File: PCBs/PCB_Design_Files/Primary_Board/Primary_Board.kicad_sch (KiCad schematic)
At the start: 6 parts, among them J1 Conn_FFC_8pin, J2 Conn_01x08_Pin

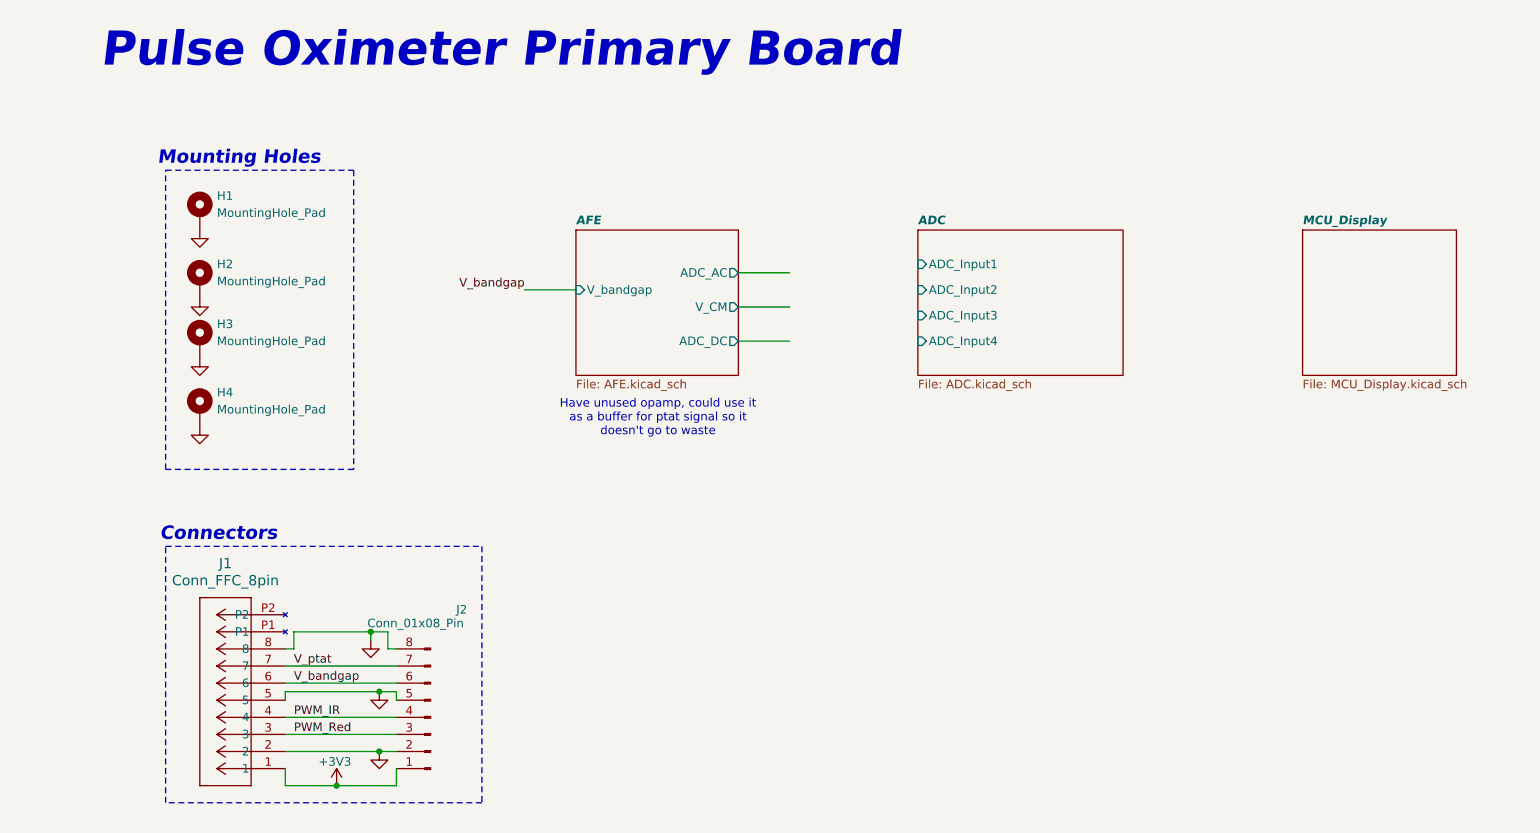
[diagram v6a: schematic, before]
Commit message: ADC schematic done
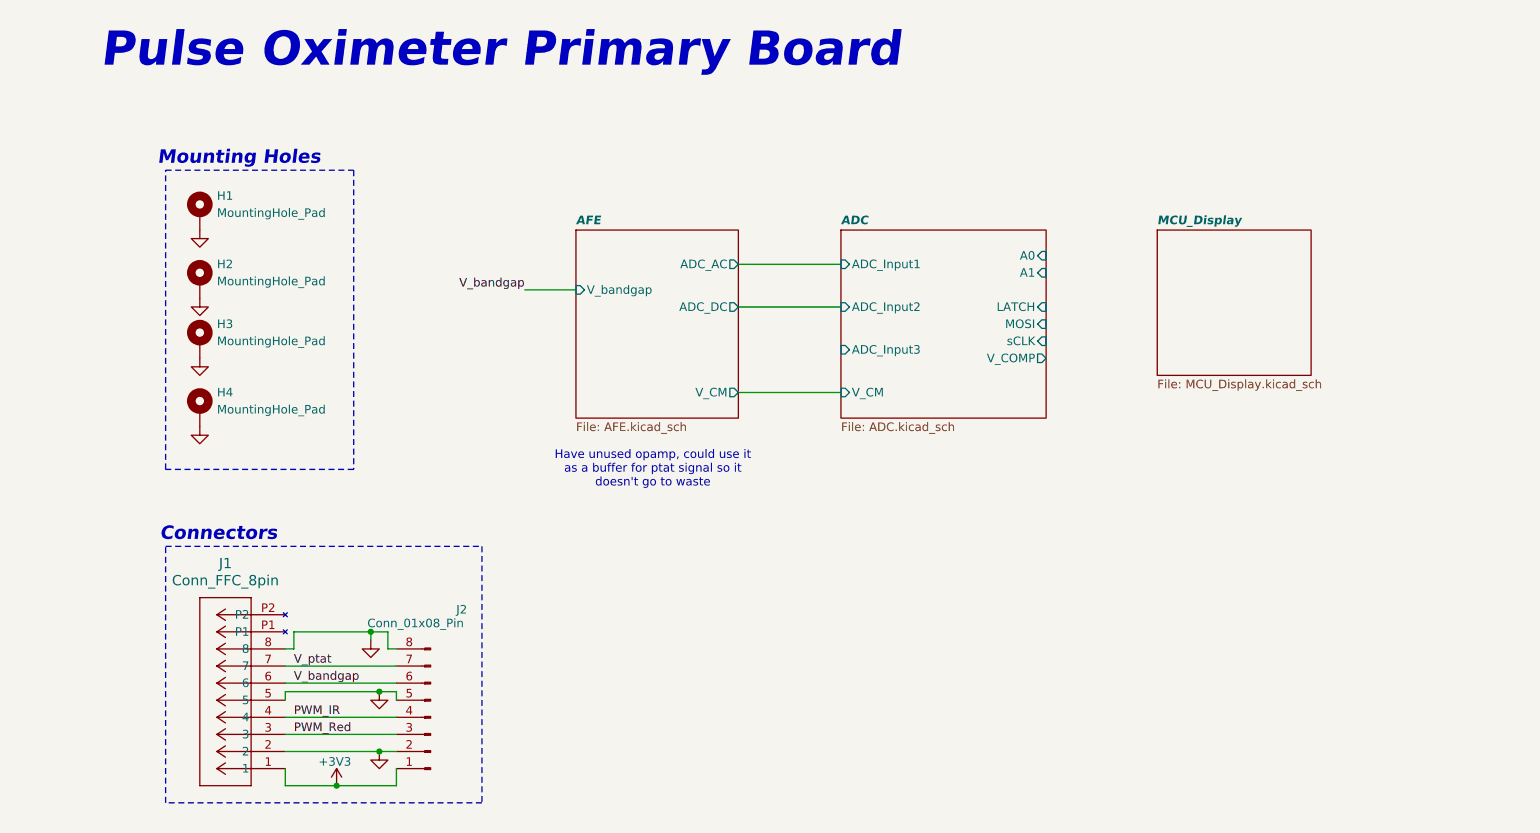
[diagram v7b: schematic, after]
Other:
- sheet ADC ports: added A0, A1, LATCH, MOSI, V_CM, V_COMP, sCLK; removed ADC_Input4
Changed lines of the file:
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@@
 	(text "Have unused opamp, could use it\nas a buffer for ptat signal so it\ndoesn't go to waste"
 		(exclude_from_sim no)
-		(at 98.552 74.93 0)
+		(at 97.79 82.55 0)
 		(effects
 			(font
@@
 	(wire
 		(pts
+			(xy 78.74 55.88) (xy 86.36 55.88)
+		)
+		(stroke
+			(width 0)
+			(type default)
+		)
+	)
+	(wire
+		(pts
 			(xy 43.18 109.22) (xy 44.45 109.22)
 		)
@@
 	(wire
 		(pts
+			(xy 110.49 58.42) (xy 125.73 58.42)
+		)
+		(stroke
+			(width 0)
+			(type default)
+		)
+	)
+	(wire
+		(pts
 			(xy 58.42 106.68) (xy 58.42 109.22)
 		)
@@
 	(wire
 		(pts
-			(xy 110.49 63.5) (xy 118.11 63.5)
-		)
-		(stroke
-			(width 0)
-			(type default)
-		)
-	)
-	(wire
-		(pts
 			(xy 43.18 114.3) (xy 59.69 114.3)
 		)
@@
 	(wire
 		(pts
-			(xy 78.74 55.88) (xy 86.36 55.88)
-		)
-		(stroke
-			(width 0)
-			(type default)
-		)
-	)
-	(wire
-		(pts
-			(xy 110.49 58.42) (xy 118.11 58.42)
+			(xy 110.49 71.12) (xy 125.73 71.12)
+		)
+		(stroke
+			(width 0)
+			(type default)
+		)
+	)
+	(wire
+		(pts
+			(xy 110.49 52.07) (xy 125.73 52.07)
 		)
 		(stroke
@@
 		(pts
 			(xy 43.18 121.92) (xy 59.69 121.92)
-		)
-		(stroke
-			(width 0)
-			(type default)
-		)
-	)
-	(wire
-		(pts
-			(xy 110.49 53.34) (xy 118.11 53.34)
 		)
 		(stroke
@@
 	(sheet
 		(at 86.36 46.99)
-		(size 24.13 21.59)
+		(size 24.13 27.94)
 		(exclude_from_sim no)
 		(in_bom yes)
@@
 		)
 		(property "Sheetfile" "AFE.kicad_sch"
-			(at 86.36 69.1646 0)
+			(at 86.36 75.5146 0)
 			(effects
 				(font
@@
 		)
 		(pin "ADC_AC" output
-			(at 110.49 53.34 0)
+			(at 110.49 52.07 0)
 			(effects
 				(font
@@
 		)
 		(pin "ADC_DC" output
-			(at 110.49 63.5 0)
+			(at 110.49 58.42 0)
 			(effects
 				(font
@@
 		)
 		(pin "V_CM" output
-			(at 110.49 58.42 0)
+			(at 110.49 71.12 0)
 			(effects
 				(font
@@
 	)
 	(sheet
-		(at 137.16 46.99)
-		(size 30.48 21.59)
+		(at 125.73 46.99)
+		(size 30.48 27.94)
 		(exclude_from_sim no)
 		(in_bom yes)
@@
 		)
 		(property "Sheetname" "ADC"
-			(at 137.16 46.2784 0)
+			(at 125.73 46.2784 0)
 			(effects
 				(font
@@
 		)
 		(property "Sheetfile" "ADC.kicad_sch"
-			(at 137.16 69.1646 0)
+			(at 125.73 75.5146 0)
 			(effects
 				(font
@@
 		)
 		(pin "ADC_Input1" input
-			(at 137.16 52.07 180)
+			(at 125.73 52.07 180)
 			(effects
 				(font
@@
 		)
 		(pin "ADC_Input2" input
-			(at 137.16 55.88 180)
+			(at 125.73 58.42 180)
 			(effects
 				(font
@@
 		)
 		(pin "ADC_Input3" input
-			(at 137.16 59.69 180)
+			(at 125.73 64.77 180)
 			(effects
 				(font
@@
 			)
 		)
-		(pin "ADC_Input4" input
-			(at 137.16 63.5 180)
+		(pin "A0" input
+			(at 156.21 50.8 0)
+			(effects
+				(font
+					(size 1.27 1.27)
+				)
+				(justify right)
+			)
+		)
+		(pin "A1" input
+			(at 156.21 53.34 0)
+			(effects
+				(font
+					(size 1.27 1.27)
+				)
+				(justify right)
+			)
+		)
+		(pin "LATCH" input
+			(at 156.21 58.42 0)
+			(effects
+				(font
+					(size 1.27 1.27)
+				)
+				(justify right)
+			)
+		)
+		(pin "MOSI" input
+			(at 156.21 60.96 0)
+			(effects
+				(font
+					(size 1.27 1.27)
+				)
+				(justify right)
+			)
+		)
+		(pin "sCLK" input
+			(at 156.21 63.5 0)
+			(effects
+				(font
+					(size 1.27 1.27)
+				)
+				(justify right)
+			)
+		)
+		(pin "V_CM" input
+			(at 125.73 71.12 180)
 			(effects
 				(font
@@
 				)
 				(justify left)
+			)
+		)
+		(pin "V_COMP" output
+			(at 156.21 66.04 0)
+			(effects
+				(font
+					(size 1.27 1.27)
+				)
+				(justify right)
 			)
 		)
@@
 	)
 	(sheet
-		(at 194.31 46.99)
+		(at 172.72 46.99)
 		(size 22.86 21.59)
 		(exclude_from_sim no)
@@
 		)
 		(property "Sheetname" "MCU_Display"
-			(at 194.31 46.2784 0)
+			(at 172.72 46.2784 0)
 			(effects
 				(font
@@
 		)
 		(property "Sheetfile" "MCU_Display.kicad_sch"
-			(at 194.31 69.1646 0)
-			(effects
-				(font
+			(at 172.72 69.1646 0)
+			(effects
+				(font

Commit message: updated bom
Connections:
- net GND: no longer J1.2, J2.2 (Pin_2)
- new net +5V: J1.2, J2.2 (Pin_2)
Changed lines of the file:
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@@
 	(rectangle
 		(start 25.4 93.98)
-		(end 72.39 132.08)
+		(end 72.39 134.62)
 		(stroke
 			(width 0)
@@
 	)
 	(junction
-		(at 50.8 129.54)
-		(diameter 0)
-		(color 0 0 0 0)
-	)
-	(junction
-		(at 57.15 124.46)
+		(at 50.8 132.08)
 		(diameter 0)
 		(color 0 0 0 0)
@@
 		(color 0 0 0 0)
 	)
+	(junction
+		(at 50.8 125.73)
+		(diameter 0)
+		(color 0 0 0 0)
+	)
 	(wire
 		(pts
@@
 	(wire
 		(pts
+			(xy 59.69 125.73) (xy 59.69 124.46)
+		)
+		(stroke
+			(width 0)
+			(type default)
+		)
+	)
+	(wire
+		(pts
 			(xy 58.42 106.68) (xy 58.42 109.22)
 		)
@@
 	(wire
 		(pts
-			(xy 57.15 124.46) (xy 59.69 124.46)
-		)
-		(stroke
-			(width 0)
-			(type default)
-		)
-	)
-	(wire
-		(pts
 			(xy 43.18 114.3) (xy 59.69 114.3)
 		)
@@
 	(wire
 		(pts
-			(xy 59.69 129.54) (xy 50.8 129.54)
+			(xy 59.69 132.08) (xy 50.8 132.08)
 		)
 		(stroke
@@
 	(wire
 		(pts
+			(xy 43.18 125.73) (xy 43.18 124.46)
+		)
+		(stroke
+			(width 0)
+			(type default)
+		)
+	)
+	(wire
+		(pts
 			(xy 44.45 106.68) (xy 55.88 106.68)
 		)
@@
 	(wire
 		(pts
-			(xy 43.18 127) (xy 43.18 129.54)
+			(xy 43.18 127) (xy 43.18 132.08)
 		)
 		(stroke
@@
 	(wire
 		(pts
-			(xy 43.18 124.46) (xy 57.15 124.46)
+			(xy 43.18 125.73) (xy 50.8 125.73)
 		)
 		(stroke
@@
 	(wire
 		(pts
+			(xy 50.8 125.73) (xy 59.69 125.73)
+		)
+		(stroke
+			(width 0)
+			(type default)
+		)
+	)
+	(wire
+		(pts
 			(xy 43.18 121.92) (xy 59.69 121.92)
 		)
@@
 	(wire
 		(pts
-			(xy 59.69 127) (xy 59.69 129.54)
-		)
-		(stroke
-			(width 0)
-			(type default)
-		)
-	)
-	(wire
-		(pts
-			(xy 43.18 129.54) (xy 50.8 129.54)
+			(xy 59.69 127) (xy 59.69 132.08)
+		)
+		(stroke
+			(width 0)
+			(type default)
+		)
+	)
+	(wire
+		(pts
+			(xy 43.18 132.08) (xy 50.8 132.08)
 		)
 		(stroke
@@
 	(symbol
 		(lib_id "power:+3V3")
-		(at 50.8 129.54 0)
+		(at 50.8 132.08 0)
 		(unit 1)
 		(exclude_from_sim no)
@@
 		(dnp no)
 		(property "Reference" "#PWR023"
-			(at 50.8 133.35 0)
+			(at 50.8 135.89 0)
 			(effects
 				(font
@@
 		)
 		(property "Value" "+3V3"
-			(at 50.546 125.984 0)
+			(at 50.546 128.524 0)
 			(effects
 				(font
@@
 		)
 		(property "Footprint" ""
-			(at 50.8 129.54 0)
+			(at 50.8 132.08 0)
 			(effects
 				(font
@@
 		)
 		(property "Datasheet" ""
-			(at 50.8 129.54 0)
+			(at 50.8 132.08 0)
 			(effects
 				(font
@@
 		)
 		(property "Description" "Power symbol creates a global label with name \"+3V3\""
-			(at 50.8 129.54 0)
+			(at 50.8 132.08 0)
 			(effects
 				(font
@@
 	)
 	(symbol
-		(lib_id "power:GND")
-		(at 57.15 124.46 0)
+		(lib_id "power:VCC")
+		(at 50.8 125.73 0)
 		(unit 1)
 		(exclude_from_sim no)
@@
 		(on_board yes)
 		(dnp no)
-		(fields_autoplaced yes)
 		(property "Reference" "#PWR026"
-			(at 57.15 130.81 0)
-			(effects
-				(font
-					(size 1.27 1.27)
-				)
-				(hide yes)
-			)
-		)
-		(property "Value" "GND"
-			(at 57.1501 128.27 90)
-			(effects
-				(font
-					(size 1.27 1.27)
-				)
-				(justify right)
-				(hide yes)
+			(at 50.8 129.54 0)
+			(effects
+				(font
+					(size 1.27 1.27)
+				)
+				(hide yes)
+			)
+		)
+		(property "Value" "+5V"
+			(at 54.61 124.46 0)
+			(effects
+				(font
+					(size 1.27 1.27)
+				)
 			)
 		)
 		(property "Footprint" ""
-			(at 57.15 124.46 0)
+			(at 50.8 125.73 0)
 			(effects
 				(font
@@
 		)
 		(property "Datasheet" ""
-			(at 57.15 124.46 0)
-			(effects
-				(font
-					(size 1.27 1.27)
-				)
-				(hide yes)
-			)
-		)
-		(property "Description" "Power symbol creates a global label with name \"GND\" , ground"
-			(at 57.15 124.46 0)
-			(effects
-				(font
+			(at 50.8 125.73 0)
+			(effects
+				(font
+					(size 1.27 1.27)
+				)
+				(hide yes)
+			)
+		)
+		(property "Description" "Power symbol creates a global label with name \"VCC\""
+			(at 50.8 125.73 0)
+			(effects
+				(font
